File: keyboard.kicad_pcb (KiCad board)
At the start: 2 copper layers, 208 parts, among them J2 USB_C_Receptacle_USB2.0_16P, J3 Conn_01x04, J4 Conn_01x05, SW1 SW_Push, SW2 SW_Push, U1 RP2040, U2 NCP1117-3.3_SOT223, U3 W25Q128JVS, U4 SRV05-4, Y1 Crystal_GND24

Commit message: HS to regular switch footprint, component layout possibly complete
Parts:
- MX1, MX10, MX11, MX12, MX13, MX14, MX15, MX16, MX17, MX18, MX19, MX2, MX20, MX21, MX22, MX23, MX24, MX25, MX26, MX27, MX28, MX29, MX3, MX30, MX31, MX33, MX34, MX35, MX36, MX37, MX38, MX39, MX4, MX40, MX41, MX42, MX43, MX44, MX46, MX48, MX49, MX5, MX50, MX51, MX52, MX53, MX54, MX55, MX56, MX57, MX58, MX59, MX6, MX60, MX61, MX62, MX63, MX64, MX65, MX66, MX67, MX68, MX69, MX7, MX70, MX71, MX73, MX74, MX78, MX79, MX8, MX80, MX81, MX82, MX83, MX84, MX9: value MX_SW_HS -> MX_SW_solder; footprint PCM_marbastlib-mx:SW_MX_HS_CPG151101S11_1u -> PCM_marbastlib-mx:SW_MX_1u; moved to F.Cu
- MX32, MX45: value MX_SW_HS -> MX_SW_solder; footprint PCM_marbastlib-mx:SW_MX_HS_CPG151101S11_1.5u -> PCM_marbastlib-mx:SW_MX_1.5u; moved to F.Cu
- MX47, MX72: value MX_SW_HS -> MX_SW_solder; footprint PCM_marbastlib-mx:SW_MX_HS_CPG151101S11_1.75u -> PCM_marbastlib-mx:SW_MX_1.75u; moved to F.Cu
- MX75, MX76, MX77: value MX_SW_HS -> MX_SW_solder; footprint PCM_marbastlib-mx:SW_MX_HS_CPG151101S11_1.25u -> PCM_marbastlib-mx:SW_MX_1.25u; moved to F.Cu
- U2: value NCP1117-3.3_SOT223 -> XC6206PxxxMR; footprint Package_TO_SOT_SMD:SOT-223-3_TabPin2 -> Package_TO_SOT_SMD:SOT-23-3
- moved R10 516.5 mm to (254.3, 127.3), turned to 90 degrees
- moved R11 515.4 mm to (253.2, 127.3), turned to 90 degrees
- moved R9 514.7 mm to (252.4, 132.6)
- moved U3 505.7 mm to (246.0, 131.3)
- moved SW2 499.8 mm to (262.0, 134.5), turned to 0 degrees
- moved R6 494.5 mm to (234.6, 147.3), turned to 135 degrees
- moved R7 493.4 mm to (227.8, 44.6), turned to -90 degrees
- moved J3 489.3 mm to (234.2, 57.2), turned to -90 degrees
- moved R1 488.2 mm to (231.8, 131.0), turned to -90 degrees
- moved R3 487.8 mm to (224.6, 44.6), turned to -90 degrees
- moved R2 487.2 mm to (230.8, 131.0), turned to -90 degrees
- moved F1 485.9 mm to (222.2, 52.4), turned to -90 degrees
- moved R8 478.8 mm to (219.1, 145.7)
- moved J2 478.4 mm to (226.0, 36.8), turned to 0 degrees
- moved U1 473.4 mm to (231.8, 138.1)
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
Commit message: component layout complete, remove 4-pin connector
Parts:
- removed J3: Conn_01x04, Connector_JST:JST_SH_SM04B-SRSS-TB_1x04-1MP_P1.00mm_Horizontal
- removed U4: SRV05-4, Package_TO_SOT_SMD:SOT-23-6
- added D85: PRTR5V0U2X, Package_TO_SOT_SMD:SOT-143, B.Cu at (225.4, 53.2)
- MX1: value MX_SW_solder -> ESC
- MX10: value MX_SW_solder -> F9
- MX11: value MX_SW_solder -> F10
- MX12: value MX_SW_solder -> F11
- MX13: value MX_SW_solder -> F12
- MX14: value MX_SW_solder -> PrtSc/NmLk
- MX15: value MX_SW_solder -> Pause/ScrLk
- MX16: value MX_SW_solder -> Delete/Insert
- MX17: value MX_SW_solder -> ~'
- MX18: value MX_SW_solder -> !1
- MX19: value MX_SW_solder -> @2
- MX2: value MX_SW_solder -> F1
- MX20: value MX_SW_solder -> #3
- MX21: value MX_SW_solder -> $4
- MX22: value MX_SW_solder -> %5
- MX23: value MX_SW_solder -> ^6
- MX24: value MX_SW_solder -> &7
- MX25: value MX_SW_solder -> *8
- MX26: value MX_SW_solder -> (9
- MX27: value MX_SW_solder -> )0
- MX28: value MX_SW_solder -> _-
- MX29: value MX_SW_solder -> +=
- MX3: value MX_SW_solder -> F2
- MX30: value MX_SW_solder -> Backspace
- MX31: value MX_SW_solder -> Home
- MX32: value MX_SW_solder -> Tab
- MX33: value MX_SW_solder -> Q
- MX34: value MX_SW_solder -> W
- MX35: value MX_SW_solder -> E
- MX36: value MX_SW_solder -> R
- MX37: value MX_SW_solder -> T
- MX38: value MX_SW_solder -> Y
- MX39: value MX_SW_solder -> U
- MX4: value MX_SW_solder -> F3
- MX40: value MX_SW_solder -> I
- MX41: value MX_SW_solder -> O
- MX42: value MX_SW_solder -> P
- MX43: value MX_SW_solder -> {[
- MX44: value MX_SW_solder -> }]
- MX45: value MX_SW_solder -> |\
- MX46: value MX_SW_solder -> PageUp
- MX47: value MX_SW_solder -> CapsLock
- MX48: value MX_SW_solder -> A
- MX49: value MX_SW_solder -> S
- MX5: value MX_SW_solder -> F4
- MX50: value MX_SW_solder -> D
- MX51: value MX_SW_solder -> F
- MX52: value MX_SW_solder -> G
- MX53: value MX_SW_solder -> H
- MX54: value MX_SW_solder -> J
- MX55: value MX_SW_solder -> K
- MX56: value MX_SW_solder -> L
- MX57: value MX_SW_solder -> :;
- MX58: value MX_SW_solder -> "'
- MX59: value MX_SW_solder -> Enter
- MX6: value MX_SW_solder -> F5
- MX60: value MX_SW_solder -> PageDown
- MX61, MX72: value MX_SW_solder -> Shift
- MX62: value MX_SW_solder -> Z
- MX63: value MX_SW_solder -> X
- MX64: value MX_SW_solder -> C
- MX65: value MX_SW_solder -> V
- MX66: value MX_SW_solder -> B
- MX67: value MX_SW_solder -> N
- MX68: value MX_SW_solder -> M
- MX69: value MX_SW_solder -> <,
- MX7: value MX_SW_solder -> F6
- MX70: value MX_SW_solder -> >.
- MX71: value MX_SW_solder -> ?/
- MX73: value MX_SW_solder -> UpArrow
- MX74: value MX_SW_solder -> End
- MX75, MX81: value MX_SW_solder -> Ctrl
- MX76: value MX_SW_solder -> Win
- MX77, MX79: value MX_SW_solder -> Alt
- MX78: value MX_SW_solder -> S[acebar
- MX8: value MX_SW_solder -> F7
- MX80: value MX_SW_solder -> Fn
- MX82: value MX_SW_solder -> LeftArrow
- MX83: value MX_SW_solder -> DownArrow
- MX84: value MX_SW_solder -> RightArrow
- MX9: value MX_SW_solder -> F8
- moved J4 13.2 mm to (215.4, 151.6), turned to -90 degrees
- moved C15 5.12 mm to (233.9, 147.3)
- moved D14 4.80 mm to (333.5, 52.4)
- moved D42 4.80 mm to (285.9, 90.5)
- moved D69 4.80 mm to (262.1, 128.6)
- moved D21 4.80 mm to (162.0, 71.4)
- moved D24 4.80 mm to (219.2, 71.4)
- moved D36 4.80 mm to (171.6, 90.5)
- moved D38 4.80 mm to (209.7, 90.5)
- moved D5 4.80 mm to (162.0, 52.4)
- moved D63 4.80 mm to (147.8, 128.6)
- moved D65 4.80 mm to (185.9, 128.6)
- moved D68 4.80 mm to (243.0, 128.6)
- moved D8 4.80 mm to (219.2, 52.4)
- moved D1 4.80 mm to (85.8, 52.4)
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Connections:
- D15 pad 1: ROW1 -> ROW0
- D16 pad 1: ROW1 -> ROW0
- D29 pad 1: ROW2 -> ROW1
- D30 pad 1: ROW2 -> ROW1
- D31 pad 1: ROW2 -> ROW1
- D43 pad 1: ROW3 -> ROW2
- D44 pad 1: ROW3 -> ROW2
- D45 pad 1: ROW3 -> ROW2
- D46 pad 1: ROW3 -> ROW2
- D57 pad 1: ROW4 -> ROW3
- D58 pad 1: ROW4 -> ROW3
- D59 pad 1: ROW4 -> ROW3
- D60 pad 1: ROW4 -> ROW3
- D71 pad 1: ROW5 -> ROW4
- D72 pad 1: ROW5 -> ROW4
- D73 pad 1: ROW5 -> ROW4
- D74 pad 1: ROW5 -> ROW4
- MX13 pad 1: COL12 -> COL11
- MX14 pad 1: COL13 -> COL12
- MX15 pad 1: COL0 -> COL13
- MX16 pad 1: COL1 -> COL14
- MX17 pad 1: COL2 -> COL0
- MX18 pad 1: COL3 -> COL1
- MX19 pad 1: COL4 -> COL2
- MX20 pad 1: COL5 -> COL3
- MX21 pad 1: COL6 -> COL4
- MX22 pad 1: COL7 -> COL5
- MX23 pad 1: COL8 -> COL6
- MX24 pad 1: COL9 -> COL7
- MX25 pad 1: COL10 -> COL8
- MX26 pad 1: COL11 -> COL9
- MX27 pad 1: COL12 -> COL10
- MX28 pad 1: COL13 -> COL11
- MX29 pad 1: COL0 -> COL12
- MX30 pad 1: COL1 -> COL13
- MX31 pad 1: COL2 -> COL14
- MX32 pad 1: COL3 -> COL0
- MX33 pad 1: COL4 -> COL1
- MX34 pad 1: COL5 -> COL2
- MX35 pad 1: COL6 -> COL3
- MX36 pad 1: COL7 -> COL4
- MX37 pad 1: COL8 -> COL5
- MX38 pad 1: COL9 -> COL6
- MX39 pad 1: COL10 -> COL7
- MX40 pad 1: COL11 -> COL8
- MX41 pad 1: COL12 -> COL9
- MX42 pad 1: COL13 -> COL10
- MX43 pad 1: COL0 -> COL11
- MX44 pad 1: COL1 -> COL12
- MX45 pad 1: COL2 -> COL13
- MX46 pad 1: COL3 -> COL14
- MX47 pad 1: COL4 -> COL0
- MX48 pad 1: COL5 -> COL1
- MX49 pad 1: COL6 -> COL2
- MX50 pad 1: COL7 -> COL3
- MX51 pad 1: COL8 -> COL4
- MX52 pad 1: COL9 -> COL5
- MX53 pad 1: COL10 -> COL6
- MX54 pad 1: COL11 -> COL7
- MX55 pad 1: COL12 -> COL8
- MX56 pad 1: COL13 -> COL9
- MX57 pad 1: COL0 -> COL10
- MX58 pad 1: COL1 -> COL11
- MX59 pad 1: COL2 -> COL13
- MX60 pad 1: COL3 -> COL14
- MX61 pad 1: COL4 -> COL0
- MX62 pad 1: COL5 -> COL1
- MX63 pad 1: COL6 -> COL2
- MX64 pad 1: COL7 -> COL3
- MX65 pad 1: COL8 -> COL4
- MX66 pad 1: COL9 -> COL5
- MX67 pad 1: COL10 -> COL6
- MX68 pad 1: COL11 -> COL7
- MX69 pad 1: COL12 -> COL8
- MX70 pad 1: COL13 -> COL9
- MX71 pad 1: COL0 -> COL10
- MX72 pad 1: COL1 -> COL11
- MX73 pad 1: COL2 -> COL13
- MX74 pad 1: COL3 -> COL14
- MX75 pad 1: COL4 -> COL0
- MX76 pad 1: COL5 -> COL1
- MX77 pad 1: COL6 -> COL2
- MX78 pad 1: COL7 -> COL5
- MX83 pad 1: COL12 -> COL13
- MX84 pad 1: COL13 -> COL14
- U1 pad 11: COL8 -> COL11
- U1 pad 13: COL10 -> COL13
- U1 pad 14: COL11 -> COL14
- U1 pad 15: COL12 -> unconnected-(U1-GPIO12-Pad15)
- U1 pad 16: COL13 -> unconnected-(U1-GPIO13-Pad16)
- U1 pad 17: ROW0 -> unconnected-(U1-GPIO14-Pad17)
- U1 pad 18: ROW1 -> unconnected-(U1-GPIO15-Pad18)
- U1 pad 2: COL0 -> ROW0
- U1 pad 27: ROW2 -> unconnected-(U1-GPIO16-Pad27)
- U1 pad 28: ROW3 -> unconnected-(U1-GPIO17-Pad28)
- U1 pad 29: ROW4 -> unconnected-(U1-GPIO18-Pad29)
- U1 pad 3: COL1 -> ROW1
- U1 pad 30: ROW5 -> unconnected-(U1-GPIO19-Pad30)
- U1 pad 31: unconnected-(U1-GPIO20-Pad31) -> ROW5
- U1 pad 32: unconnected-(U1-GPIO21-Pad32) -> COL0
- U1 pad 34: unconnected-(U1-GPIO22-Pad34) -> COL1
- U1 pad 35: unconnected-(U1-GPIO23-Pad35) -> COL2
- U1 pad 36: unconnected-(U1-GPIO24-Pad36) -> COL3
- U1 pad 37: unconnected-(U1-GPIO25-Pad37) -> COL4
- U1 pad 38: unconnected-(U1-GPIO26/ADC0-Pad38) -> COL5
- U1 pad 39: unconnected-(U1-GPIO27/ADC1-Pad39) -> COL6
- U1 pad 4: COL2 -> ROW2
- U1 pad 40: unconnected-(U1-GPIO28/ADC2-Pad40) -> ROW4
- U1 pad 41: unconnected-(U1-GPIO29/ADC3-Pad41) -> ROW3
- U1 pad 5: COL3 -> unconnected-(U1-GPIO3-Pad5)
- U1 pad 6: COL4 -> COL7
- U1 pad 7: COL5 -> COL8
- U1 pad 8: COL6 -> COL10
- U1 pad 9: COL7 -> COL12
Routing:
- net COL11: track 0.00 -> 130.1 mm
- net COL1: track 0.00 -> 113.0 mm
- net COL9: track 0.00 -> 111.0 mm
- net COL8: track 0.00 -> 111.0 mm
- net COL10: track 0.00 -> 111.0 mm
- net COL2: track 0.00 -> 110.0 mm
- net COL13: track 0.00 -> 109.1 mm
- net COL5: track 0.00 -> 106.1 mm
- net COL0: track 0.00 -> 105.3 mm
- net /USB_D-: track 0.00 -> 103.8 mm
- net /USB_D+: track 0.00 -> 102.7 mm
- net COL7: track 0.00 -> 86.1 mm
- net COL6: track 0.00 -> 86.1 mm
- net COL4: track 0.00 -> 86.1 mm
- net COL3: track 0.00 -> 86.1 mm
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- added copper zone on B.Cu, net GND
- added copper zone on F.Cu, net GND
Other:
- board outline added: 304.8 x 119.1 mm

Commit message: add traces to usb subcircuit and subtraces
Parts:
- R1, R10, R11, R2, R6, R8, R9: footprint Resistor_SMD:R_0402_1005Metric -> Resistor_SMD:R_0402_1005Metric_Pad0.72x0.64mm_HandSolder
- R3, R7: footprint Resistor_SMD:R_0402_1005Metric -> Resistor_SMD:R_0805_2012Metric_Pad1.20x1.40mm_HandSolder
- moved F1 4.25 mm to (222.2, 53.2)
- moved R7 1.75 mm to (222.2, 45.4), turned to 180 degrees
- moved R3 0.90 mm to (227.8, 46.0)
- turned D85 to 180 degrees
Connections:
- D85 pad 2: /USB_D- -> /USB_D+
- D85 pad 3: /USB_D+ -> /USB_D-
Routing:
- net +5V: track 0.00 -> 71.2 mm
- net VBUS: track 0.00 -> 19.7 mm, vias 0 -> 2
- net +3V3: track 0.00 -> 18.8 mm
- net Net-(J2-CC1): track 0.00 -> 4.35 mm
- net Net-(J2-CC2): track 0.00 -> 4.02 mm
- net GND: track 0.00 -> 0.53 mm

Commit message: routing complete, need to run DRC
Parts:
- moved SW2 19.4 mm to (255.9, 116.3)
- moved R9 8.48 mm to (250.6, 123.0), turned to -90 degrees
- moved R11 7.07 mm to (247.7, 125.4)
- moved R10 5.72 mm to (250.0, 126.0), turned to 180 degrees
- moved R1 3.54 mm to (231.2, 128.4)
- moved R2 3.54 mm to (230.2, 128.4)
- moved C7 1.72 mm to (238.9, 134.9)
- moved C2 1.12 mm to (233.8, 131.9)
- moved C8 1.12 mm to (232.8, 131.9)
- moved C10 1.12 mm to (231.8, 131.9)
- moved C14 1.05 mm to (224.6, 140.2)
- moved U3 0.84 mm to (249.2, 129.8), turned to 180 degrees
- moved C11 0.53 mm to (231.3, 145.4)
- moved C3 0.53 mm to (230.3, 145.4)
- moved C15 0.26 mm to (233.9, 147.6)
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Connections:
- J4 pad 4: /SWC -> /SWD
- J4 pad 5: /SWD -> /SWC
- U1 pad 11: COL11 -> unconnected-(U1-GPIO8-Pad11)
- U1 pad 12: COL9 -> unconnected-(U1-GPIO9-Pad12)
- U1 pad 13: COL13 -> COL8
- U1 pad 14: COL14 -> COL9
- U1 pad 15: unconnected-(U1-GPIO12-Pad15) -> COL10
- U1 pad 16: unconnected-(U1-GPIO13-Pad16) -> COL11
- U1 pad 17: unconnected-(U1-GPIO14-Pad17) -> COL13
- U1 pad 18: unconnected-(U1-GPIO15-Pad18) -> COL14
- U1 pad 2: ROW0 -> COL7
- U1 pad 28: unconnected-(U1-GPIO17-Pad28) -> ROW5
- U1 pad 29: unconnected-(U1-GPIO18-Pad29) -> COL5
- U1 pad 3: ROW1 -> unconnected-(U1-GPIO1-Pad3)
- U1 pad 31: ROW5 -> unconnected-(U1-GPIO20-Pad31)
- U1 pad 32: COL0 -> unconnected-(U1-GPIO21-Pad32)
- U1 pad 34: COL1 -> COL0
- U1 pad 35: COL2 -> COL1
- U1 pad 36: COL3 -> COL2
- U1 pad 37: COL4 -> COL3
- U1 pad 38: COL5 -> COL4
- U1 pad 39: COL6 -> ROW3
- U1 pad 4: ROW2 -> unconnected-(U1-GPIO2-Pad4)
- U1 pad 40: ROW4 -> COL6
- U1 pad 41: ROW3 -> ROW4
- U1 pad 6: COL7 -> COL12
- U1 pad 7: COL8 -> ROW2
- U1 pad 8: COL10 -> ROW1
- U1 pad 9: COL12 -> ROW0
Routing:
- net ROW0: track 0.00 -> 495.9 mm, vias 0 -> 4
- net ROW1: track 0.00 -> 477.4 mm, vias 0 -> 4
- net ROW2: track 0.00 -> 454.1 mm, vias 0 -> 6
- net ROW3: track 0.00 -> 317.8 mm, vias 0 -> 6
- net ROW5: track 0.00 -> 308.8 mm, vias 0 -> 2
- net ROW4: track 0.00 -> 286.8 mm, vias 0 -> 3
- net COL14: track 76.2 -> 239.9 mm, vias 0 -> 1
- net COL0: track 105.3 -> 247.4 mm, vias 0 -> 1
- net COL12: track 50.9 -> 181.8 mm, vias 0 -> 3
- net COL13: track 109.1 -> 233.4 mm, vias 0 -> 1
- net COL1: track 113.0 -> 230.7 mm, vias 0 -> 1
- net COL11: track 130.1 -> 234.7 mm, vias 0 -> 1
- net +3V3: track 18.8 -> 114.3 mm, vias 0 -> 11
- net COL2: track 110.0 -> 201.6 mm, vias 0 -> 1
- net COL10: track 111.0 -> 195.6 mm, vias 0 -> 1
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
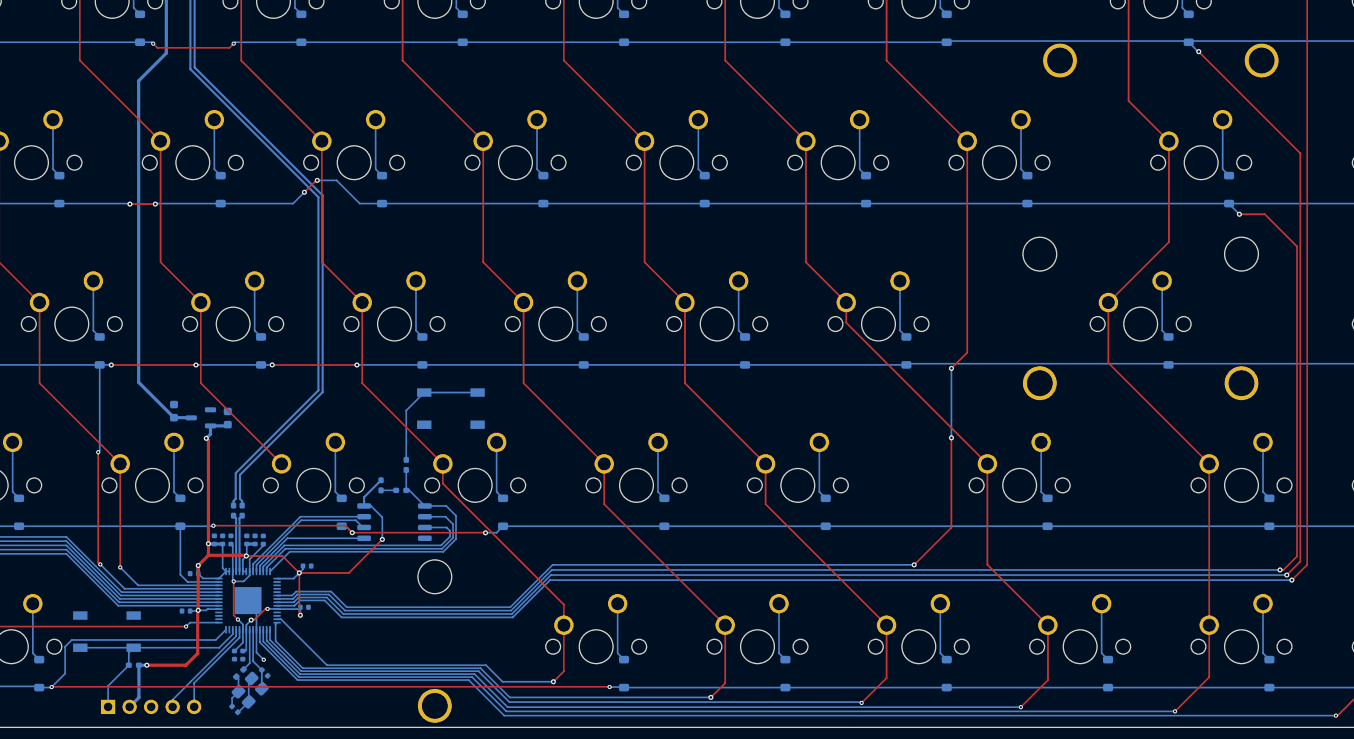
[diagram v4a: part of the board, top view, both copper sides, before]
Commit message: clean up schematic
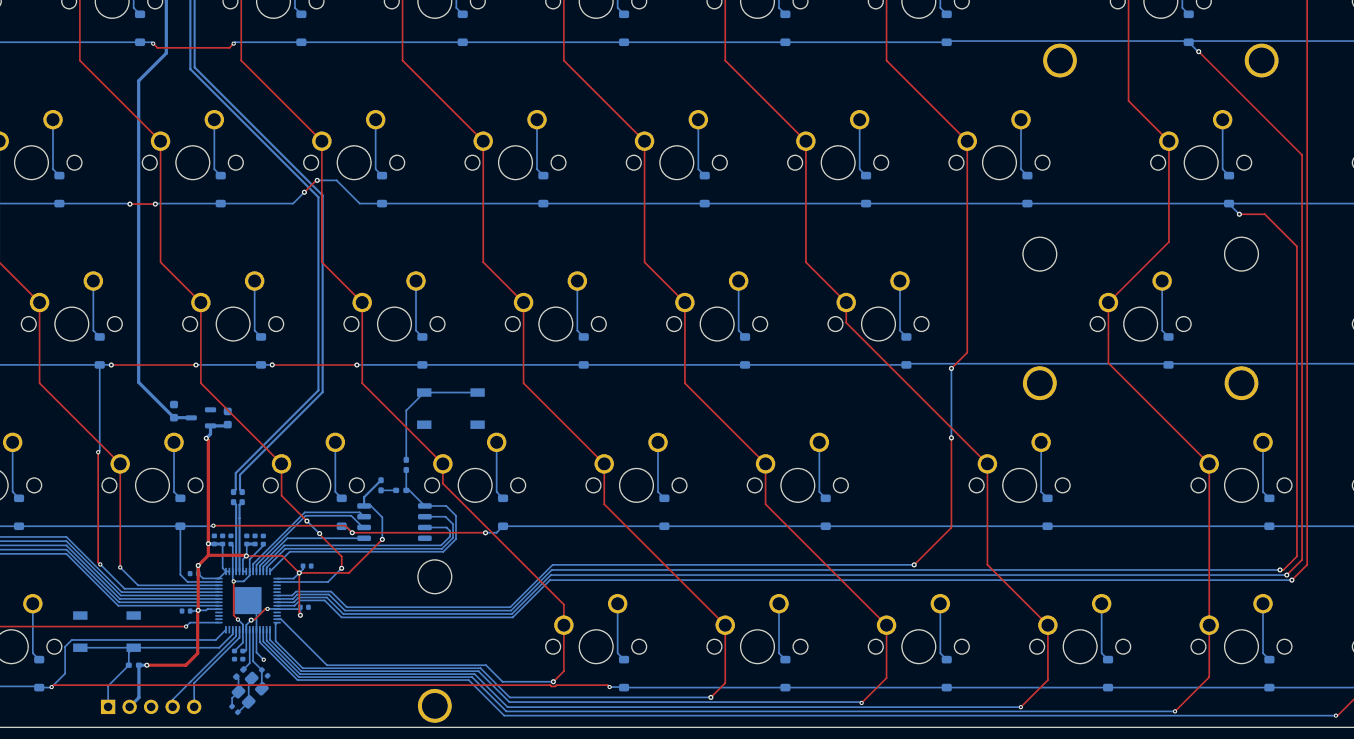
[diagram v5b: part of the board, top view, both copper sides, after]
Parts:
- moved R1 1.59 mm to (231.2, 126.8)
- moved R2 1.59 mm to (230.2, 126.8)
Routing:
- net COL7: track 86.1 -> 109.6 mm, vias 0 -> 3
- net Net-(U1-USB_DP): track 6.72 -> 8.31 mm
- net Net-(U1-USB_DM): track 6.78 -> 8.37 mm
- net /USB_D-: track 100.6 -> 99.0 mm
- net /USB_D+: track 99.5 -> 97.9 mm
